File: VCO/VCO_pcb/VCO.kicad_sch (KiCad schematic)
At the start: 66 parts, among them J1 Thonkiconn, J2 Thonkiconn, J3 Thonkiconn, J4 Thonkiconn, J5 Thonkiconn, Q1 BCM847BS,115, Q2 MMBFJ111, U1 TL074, U2 TL074, U3 TL072

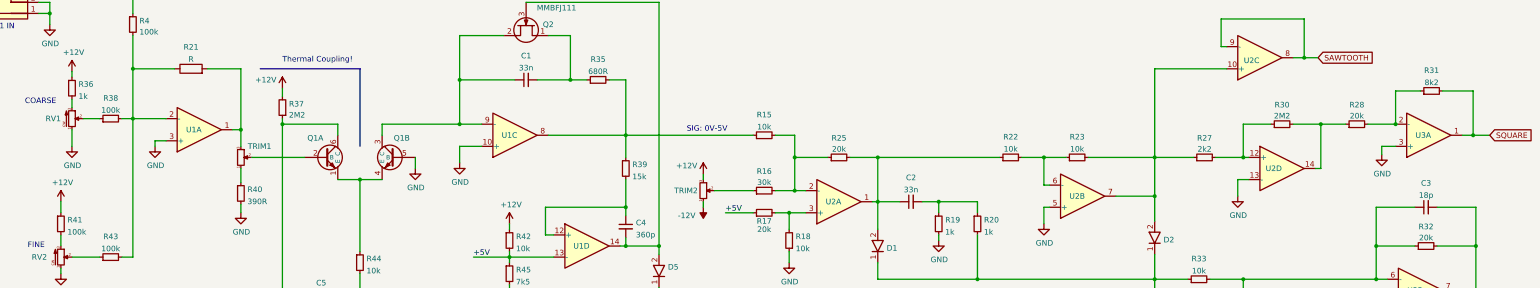
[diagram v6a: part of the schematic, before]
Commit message: final minor value changes
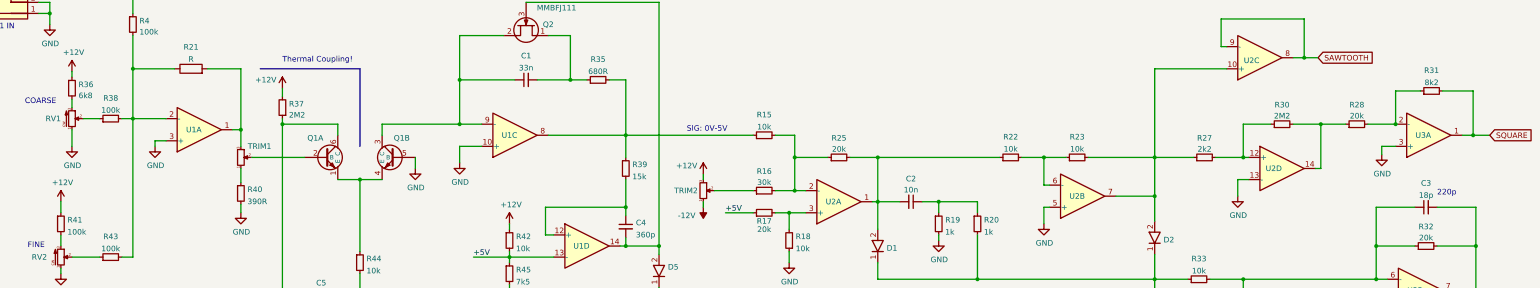
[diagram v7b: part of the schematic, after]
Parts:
- removed C2: 33n, passive_parts:C_0603_1608Metric, symbol capacitor_mlcc_0603:33n
- removed R36: 1k, passive_parts:R_0603_1608Metric, symbol resistor_0603:1k
- added C2: 10n, passive_parts:C_0603_1608Metric, symbol capacitor_mlcc_0603:10n
- added R36: 6k8, passive_parts:R_0603_1608Metric, symbol resistor_0603:6k8
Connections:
- net +12V: now also R36.1
- net at R19.1, R20.1: now also C2.1
- net at D1.2, R22.1, R25.2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: now also C2.2
- net at RV1.3: now also R36.2
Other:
- note added: "220p"
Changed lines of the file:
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@@
     (stroke (width 0) (type default) (color 0 0 0 0))
   )
+  (text "220p\n" (at 360.045 108.585 0)
+    (effects (font (size 1.27 1.27)) (justify left bottom))
+  )
   (text "CV1 IN" (at 27.94 70.485 0)
     (effects (font (size 1.27 1.27)) (justify left bottom))
@@
     (pin "3")
   )
+  (symbol (lib_id "capacitor_mlcc_0603:10n") (at 239.395 109.855 270) (unit 1)
+    (in_bom yes) (on_board yes) (fields_autoplaced)
+    (property "Reference" "C2" (id 0) (at 239.3886 104.5931 90))
+    (property "Value" "10n" (id 1) (at 239.3886 107.13 90))
+    (property "Footprint" "passive_parts:C_0603_1608Metric" (id 2) (at 255.905 136.525 0)
+      (effects (font (size 1.27 1.27)) hide)
+    )
+    (property "Datasheet" "http://www.passivecomponent.com/wp-content/uploads/datasheet/WTC_MLCC_General_Purpose.pdf" (id 3) (at 253.365 121.285 0)
+      (effects (font (size 1.27 1.27)) hide)
+    )
+    (property "Voltage" "50V" (id 4) (at 234.315 112.395 0)
+      (effects (font (size 1.27 1.27)) hide)
+    )
+    (property "Dielectric" "X7R" (id 5) (at 250.825 121.285 0)
+      (effects (font (size 1.27 1.27)) hide)
+    )
+    (property "Tolerance" "5%" (id 6) (at 248.285 121.285 0)
+      (effects (font (size 1.27 1.27)) hide)
+    )
+    (property "MFN" "Walsin Technology Corporation" (id 7) (at 245.745 121.285 0)
+      (effects (font (size 1.27 1.27)) hide)
+    )
+    (property "MPN" "0603B103J500CT" (id 8) (at 243.205 121.285 0)
+      (effects (font (size 1.27 1.27)) hide)
+    )
+    (property "LCSC" "~" (id 9) (at 240.665 121.285 0)
+      (effects (font (size 1.27 1.27)) hide)
+    )
+    (pin "1")
+    (pin "2")
+  )
   (symbol (lib_id "resistor_0603:18k") (at 295.275 132.715 0) (unit 1)
     (in_bom yes) (on_board yes) (fields_autoplaced)
@@
     (pin "3")
   )
+  (symbol (lib_id "resistor_0603:6k8") (at 46.99 83.82 0) (unit 1)
+    (in_bom yes) (on_board yes) (fields_autoplaced)
+    (property "Reference" "R36" (id 0) (at 48.4886 82.9853 0)
+      (effects (font (size 1.27 1.27)) (justify left))
+    )
+    (property "Value" "6k8" (id 1) (at 48.4886 85.5222 0)
+      (effects (font (size 1.27 1.27)) (justify left))
+    )
+    (property "Footprint" "passive_parts:R_0603_1608Metric" (id 2) (at 71.12 63.5 0)
+      (effects (font (size 1.27 1.27)) hide)
+    )
+    (property "Datasheet" "https://www.bourns.com/docs/product-datasheets/cr.pdf?sfvrsn=574d41f6_14" (id 3) (at 55.88 67.31 0)
+      (effects (font (size 1.27 1.27)) (justify left) hide)
+    )
+    (property "MFN" "Bourns Inc." (id 4) (at 55.88 69.85 0)
+      (effects (font (size 1.27 1.27)) (justify left) hide)
+    )
+    (property "MPN" "CR0603-FX-6801ELF" (id 5) (at 55.88 72.39 0)
+      (effects (font (size 1.27 1.27)) (justify left) hide)
+    )
+    (property "Tolerance" "1%" (id 6) (at 55.88 74.93 0)
+      (effects (font (size 1.27 1.27)) (justify left) hide)
+    )
+    (property "Power" "1/10W" (id 7) (at 55.88 77.47 0)
+      (effects (font (size 1.27 1.27)) (justify left) hide)
+    )
+    (property "LCSC" "~" (id 8) (at 55.88 80.01 0)
+      (effects (font (size 1.27 1.27)) (justify left) hide)
+    )
+    (pin "1")
+    (pin "2")
+  )
   (symbol (lib_id "resistor_0603:15k") (at 173.99 102.235 0) (unit 1)
     (in_bom yes) (on_board yes) (fields_autoplaced)
@@
     (pin "2")
   )
-  (symbol (lib_id "capacitor_mlcc_0603:33n") (at 239.395 109.855 90) (unit 1)
-    (in_bom yes) (on_board yes) (fields_autoplaced)
-    (property "Reference" "C2" (id 0) (at 239.4013 104.3264 90))
-    (property "Value" "33n" (id 1) (at 239.4013 107.1015 90))
-    (property "Footprint" "passive_parts:C_0603_1608Metric" (id 2) (at 222.885 83.185 0)
-      (effects (font (size 1.27 1.27)) hide)
-    )
-    (property "Datasheet" "https://media.digikey.com/pdf/Data%20Sheets/Samsung%20PDFs/CL10B333KB8NNNC_Spec.pdf" (id 3) (at 225.425 98.425 0)
-      (effects (font (size 1.27 1.27)) hide)
-    )
-    (property "Voltage" "50V" (id 4) (at 244.475 107.315 0)
-      (effects (font (size 1.27 1.27)) hide)
-    )
-    (property "Dielectric" "X7R" (id 5) (at 227.965 98.425 0)
-      (effects (font (size 1.27 1.27)) hide)
-    )
-    (property "Tolerance" "10%" (id 6) (at 230.505 98.425 0)
-      (effects (font (size 1.27 1.27)) hide)
-    )
-    (property "MFN" "Samsung Electro-Mechanics" (id 7) (at 233.045 98.425 0)
-      (effects (font (size 1.27 1.27)) hide)
-    )
-    (property "MPN" "CL10B333KB8NNNC" (id 8) (at 235.585 98.425 0)
-      (effects (font (size 1.27 1.27)) hide)
-    )
-    (property "LCSC" "~" (id 9) (at 238.125 98.425 0)
-      (effects (font (size 1.27 1.27)) hide)
-    )
-    (pin "1")
-    (pin "2")
-  )
   (symbol (lib_id "capacitor_mlcc_0603:18p") (at 357.505 111.125 90) (unit 1)
     (in_bom yes) (on_board yes) (fields_autoplaced)
@@
     (pin "4")
   )
-  (symbol (lib_id "resistor_0603:1k") (at 46.99 83.82 0) (unit 1)
-    (in_bom yes) (on_board yes) (fields_autoplaced)
-    (property "Reference" "R36" (id 0) (at 48.4886 82.9115 0)
-      (effects (font (size 1.27 1.27)) (justify left))
-    )
-    (property "Value" "1k" (id 1) (at 48.4886 85.6866 0)
-      (effects (font (size 1.27 1.27)) (justify left))
-    )
-    (property "Footprint" "passive_parts:R_0603_1608Metric" (id 2) (at 71.12 63.5 0)
-      (effects (font (size 1.27 1.27)) hide)
-    )
-    (property "Datasheet" "https://www.bourns.com/docs/product-datasheets/cr.pdf?sfvrsn=574d41f6_14" (id 3) (at 55.88 67.31 0)
-      (effects (font (size 1.27 1.27)) (justify left) hide)
-    )
-    (property "MFN" "Bourns" (id 4) (at 55.88 69.85 0)
-      (effects (font (size 1.27 1.27)) (justify left) hide)
-    )
-    (property "MPN" "CR0603-FX-1001ELF" (id 5) (at 55.88 72.39 0)
-      (effects (font (size 1.27 1.27)) (justify left) hide)
-    )
-    (property "Tolerance" "1%" (id 6) (at 55.88 74.93 0)
-      (effects (font (size 1.27 1.27)) (justify left) hide)
-    )
-    (property "Power" "1/10" (id 7) (at 55.88 77.47 0)
-      (effects (font (size 1.27 1.27)) (justify left) hide)
-    )
-    (property "LCSC" "~" (id 8) (at 55.88 80.01 0)
-      (effects (font (size 1.27 1.27)) (justify left) hide)
-    )
-    (pin "1")
-    (pin "2")
-  )
   (symbol (lib_id "resistor_0603:100k") (at 55.88 122.555 90) (unit 1)
     (in_bom yes) (on_board yes) (fields_autoplaced)
@@
       (reference "C1") (unit 1) (value "33n") (footprint "passive_parts:C_0603_1608Metric")
     )
-    (path "/ca6fd445-25fc-4651-83d7-97f98c16de03"
-      (reference "C2") (unit 1) (value "33n") (footprint "passive_parts:C_0603_1608Metric")
+    (path "/86ed0075-acf3-4a2d-8d62-5ec053ce725b"
+      (reference "C2") (unit 1) (value "10n") (footprint "passive_parts:C_0603_1608Metric")
     )
     (path "/cc16a96b-0dad-4cfe-b8dc-c513388cc4ea"
@@
       (reference "R35") (unit 1) (value "680R") (footprint "passive_parts:R_0603_1608Metric")
     )
-    (path "/e8764411-3e8d-4bb5-a520-6ed6e0721270"
-      (reference "R36") (unit 1) (value "1k") (footprint "passive_parts:R_0603_1608Metric")
+    (path "/ac023325-14ac-4b82-b3e4-c81a75691d71"
+      (reference "R36") (unit 1) (value "6k8") (footprint "passive_parts:R_0603_1608Metric")
     )
     (path "/4e7ad0e3-9de8-4b55-b80a-02c2d08ad493"
